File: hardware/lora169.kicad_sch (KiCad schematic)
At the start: 0 parts

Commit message: Avancement schéma et PCB carte mère lora169
Schéma : pose XIAO ESP32-S3 et E22-170M30S, condensateurs de découplage
100nF + 10µF sur le rail VCC du E22, labels de signaux pour les
liaisons SPI/IO entre les deux modules, power ports +3V3/GND avec
PWR_FLAG sur les rails alim. NC flags posés sur les pins volontairement
non connectées (E22 DIO2 et ANT en version IPEX, XIAO D5/D6/VBUS).

PCB : empreintes importées depuis le schéma, placement initial des
quatre composants, contour de carte tracé sur Edge.Cuts, début de
routage des liaisons signal et alim. Reste le passage de l'alim VCC E22
de 3V3 à VBUS pour permettre le 30 dBm hardware (à faire dans un commit
suivant après remplacement du E22 soudé direct par les embases femelles
qui recevront le breakout).

Co-Authored-By: Claude Opus 4.7 (1M context) <noreply@anthropic.com>
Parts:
- added C1: 100nF, Capacitor_SMD:C_0805_2012Metric, symbol Device:C_Small
- added C2: 10uF, Capacitor_SMD:C_0805_2012Metric, symbol Device:C_Small
- added U1: XIAO-ESP32-S3-DIP, Seeed_XIAO:XIAO-ESP32-S3-DIP, symbol Seeed_XIAO:XIAO-ESP32-S3-DIP
- added U2: E22-170M30S-SX1262, Ebyte_E22:E22-170M30S-SX1262, symbol Ebyte_E22:E22-170M30S-SX1262
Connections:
- new net +3V3: C1.1, C2.1, U1.12 (3V3), U2.10 (VCC), U2.9 (VCC)
- new net BUSY: U1.3 (GPIO3_A2_D2), U2.14 (BUSY)
- new net DIO1: U1.2 (GPIO2_A1_D1), U2.13 (DIO1)
- new net GND: C1.2, C2.2, U1.13 (GND), U2.1 (GND), U2.11 (GND), U2.12 (GND), U2.2 (GND), U2.20 (GND), U2.22 (GND), U2.3 (GND), U2.4 (GND), U2.5 (GND)
- new net MISO: U1.10 (GPIO8_A9_D9_MISO), U2.16 (MISO)
- new net MOSI: U1.11 (GPIO9_A10_D10_MOSI), U2.17 (MOSI)
- new net NRST: U1.1 (GPIO1_A0_D0), U2.15 (NRST)
- new net NSS: U1.8 (GPIO44_D7_RX), U2.19 (NSS)
- new net RXEN: U1.5 (GPIO5_A4_D4_SDA), U2.6 (RXEN)
- new net SCK: U1.9 (GPIO7_A8_D8_SCK), U2.18 (SCK)
- new net TXEN: U1.4 (GPIO4_A3_D3), U2.7 (TXEN)
- no-connect marks 0 -> 5

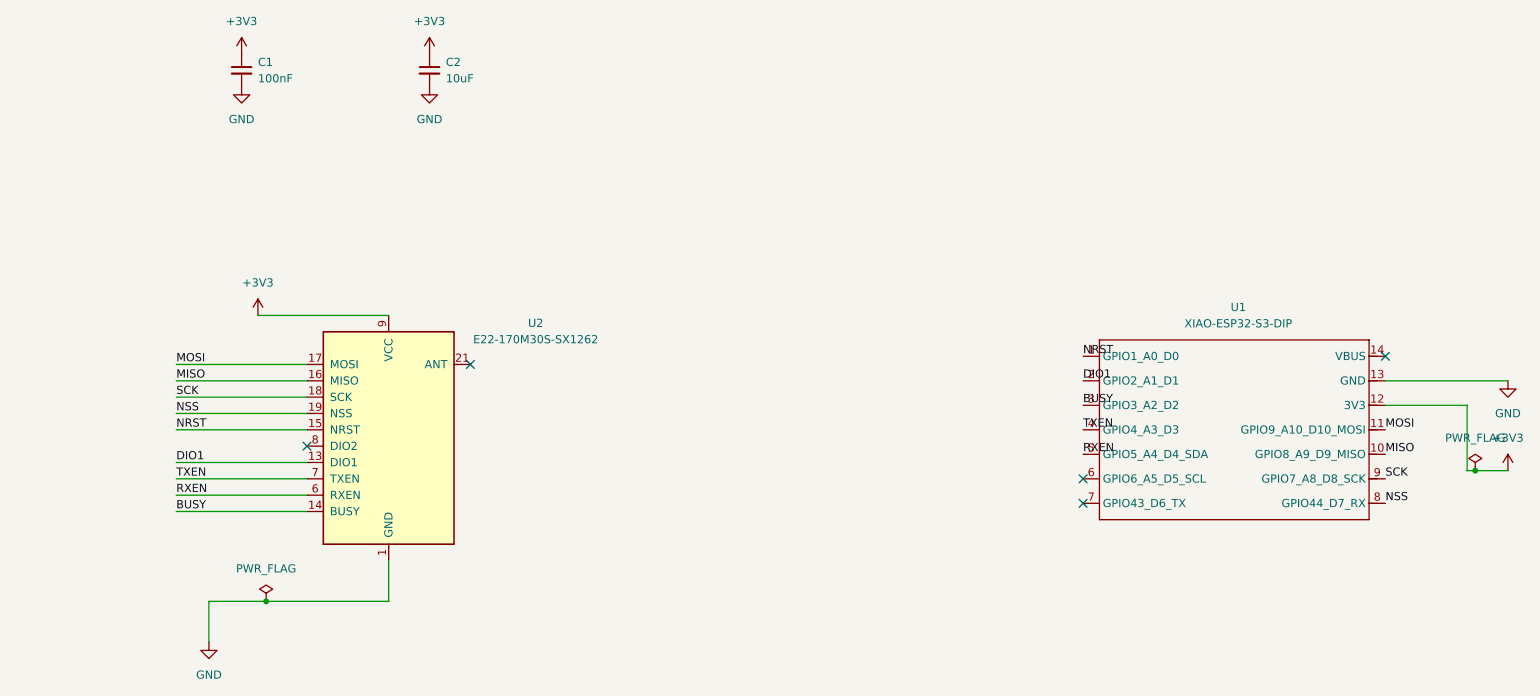
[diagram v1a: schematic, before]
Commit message: Refonte from scratch carte mère adaptée au breakout E22 + finitions
Carte mère reconçue pour recevoir le breakout E22 plutôt que le module
soudé direct. Trois composants seulement : XIAO ESP32-S3 DIP, plus
deux embases femelles 1×11 (PinSocket_2.54mm) espacées de 32,1 mm
centre à centre pour matcher les pin headers du breakout.

Schéma : labels signaux (NRST, DIO1, BUSY, TXEN, RXEN, NSS, SCK, MISO,
MOSI), power ports +5V (au lieu de +3V3) sur la pin VBUS du XIAO et
les broches VCC du connecteur — alimentation passe maintenant par
VBUS pour permettre la pleine puissance 30 dBm hardware. NC flags sur
DIO2, ANT, et pins XIAO réserve.

PCB compact 80 × 55 mm avec contour Edge.Cuts, USB-C du XIAO en bord
gauche pour découpe boîtier simple. Routage manuel en F.Cu pour
préserver la continuité du plan de masse face arrière, avec inversions
MISO↔MOSI et NRST↔DIO1 dans le firmware pour éliminer les croisements
géométriques. Zones GND coulées sur F.Cu et B.Cu en mode pleine
connexion.

DRC : 0 erreur, 0 pad non connecté. Les warnings restants sont
purement cosmétiques (silkscreen XIAO qui dépasse du bord PCB côté
USB-C — attendu).

Breakout E22 : ajustements mineurs après finalisation du DRC.

.gitignore élargi : **/fab/ pour ignorer les Gerbers de tous les
sous-projets, *-gerbers.zip pour les ZIP d'upload, *.dsn / *.ses pour
les intermédiaires Freerouting.

Co-Authored-By: Claude Opus 4.7 (1M context) <noreply@anthropic.com>
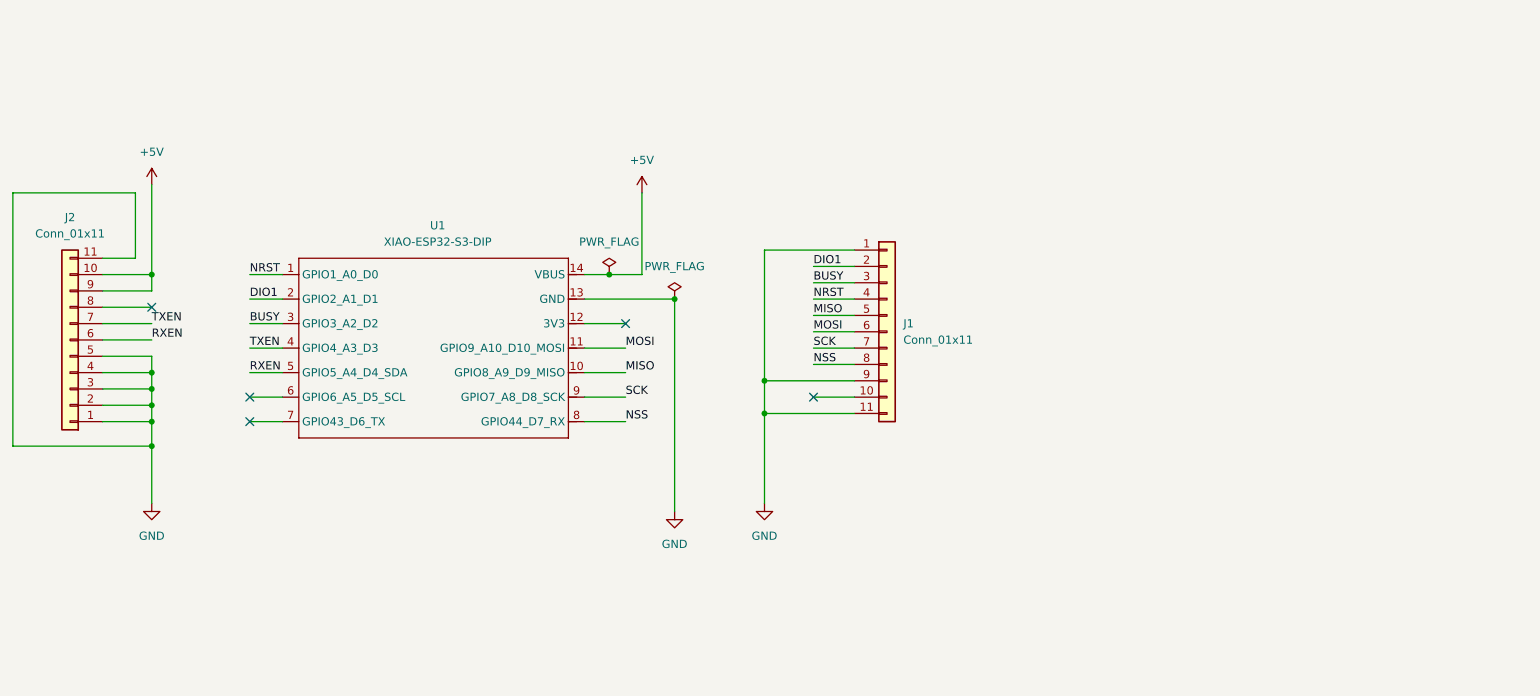
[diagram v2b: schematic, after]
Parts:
- removed C1: 100nF, Capacitor_SMD:C_0805_2012Metric, symbol Device:C_Small
- removed C2: 10uF, Capacitor_SMD:C_0805_2012Metric, symbol Device:C_Small
- removed U2: E22-170M30S-SX1262, Ebyte_E22:E22-170M30S-SX1262, symbol Ebyte_E22:E22-170M30S-SX1262
- added J1, J2: Conn_01x11, Connector_PinSocket_2.54mm:PinSocket_1x11_P2.54mm_Vertical, symbol Connector_Generic:Conn_01x11
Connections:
- net BUSY: now also J1.3 (Pin_3)
- net DIO1: now also J1.2 (Pin_2)
- net GND: now also J1.1 (Pin_1), J1.11 (Pin_11), J1.9 (Pin_9), J2.1 (Pin_1), J2.11 (Pin_11), J2.2 (Pin_2), J2.3 (Pin_3), J2.4 (Pin_4), J2.5 (Pin_5)
- net MISO: now also J1.5 (Pin_5)
- net MOSI: now also J1.6 (Pin_6)
- net NRST: now also J1.4 (Pin_4)
- net NSS: now also J1.8 (Pin_8)
- net RXEN: now also J2.6 (Pin_6)
- net SCK: now also J1.7 (Pin_7)
- net TXEN: now also J2.7 (Pin_7)
- net +5V: now reaches U1.14 (VBUS)
- net +5V: now also J2.10 (Pin_10), J2.9 (Pin_9)
- net +3V3: no longer names the net of U1.12 (3V3)
